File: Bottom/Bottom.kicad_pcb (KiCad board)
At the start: 2 copper layers, 40 x 40 mm, 32 parts, among them M1 Motor, M2 Motor, U1 GP2S60, U2 GP2S60, U7 DRV8833PWP

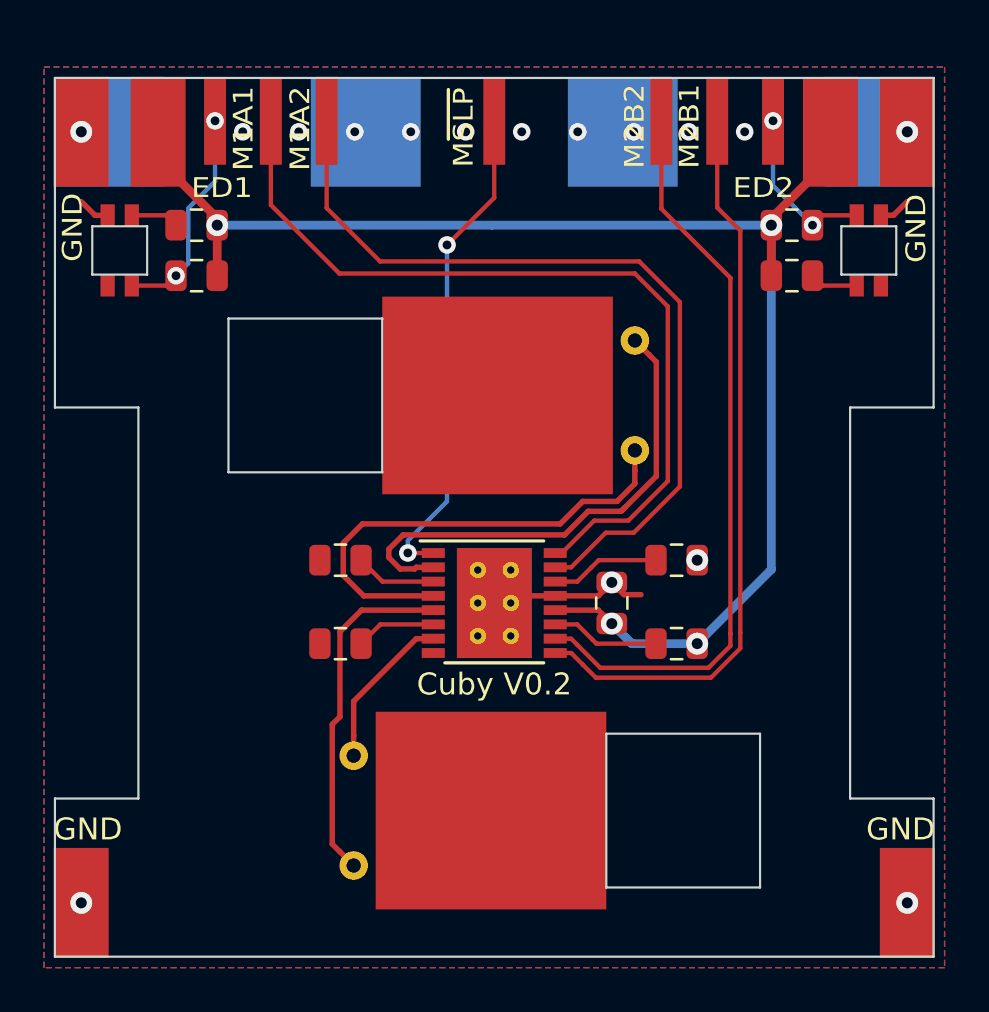
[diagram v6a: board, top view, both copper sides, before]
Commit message: removed extra pins in front, respaced pins in bottom and front
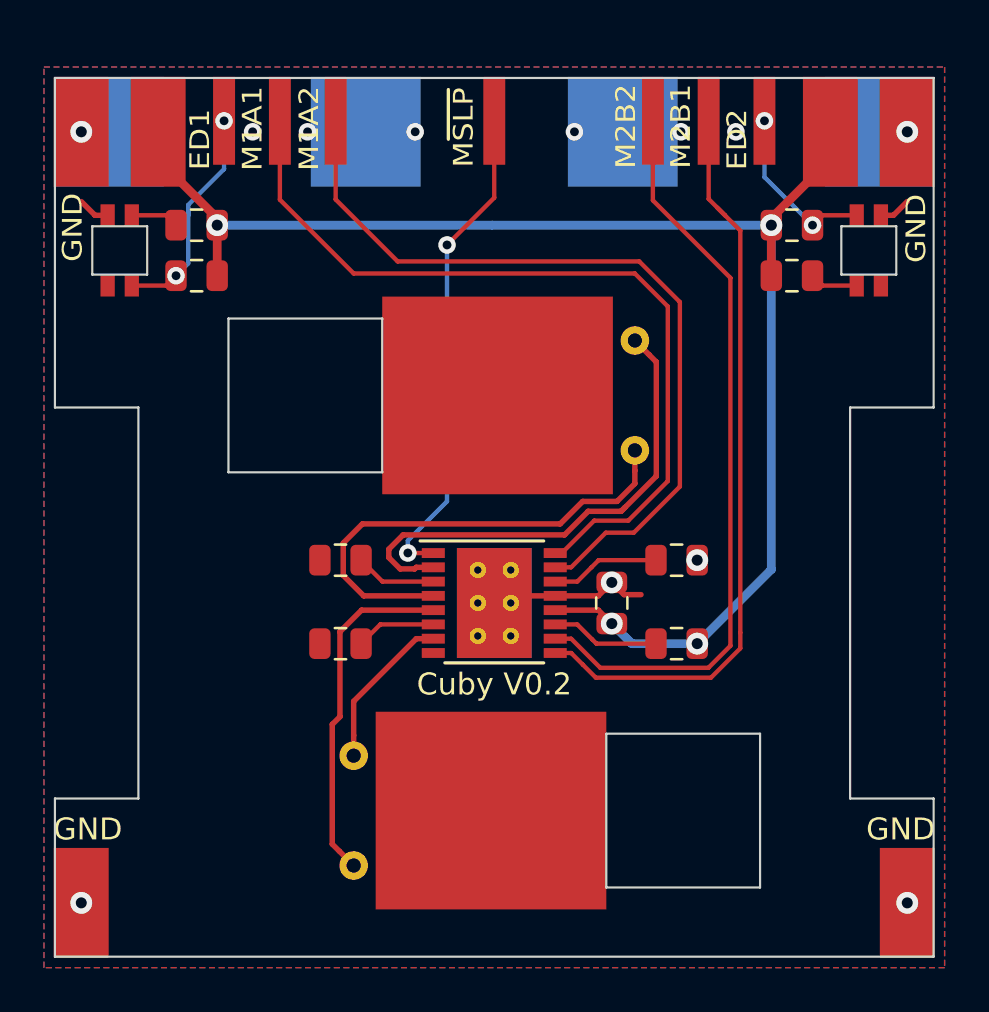
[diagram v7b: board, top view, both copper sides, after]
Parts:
- moved H1 0.41 mm to (163.2, 80.0)
- moved H2 0.41 mm to (165.8, 80.0)
- moved H5 0.41 mm to (160.7, 80.0)
- moved H3 0.39 mm to (182.8, 80.0)
- moved H4 0.39 mm to (180.2, 80.0)
- moved H6 0.39 mm to (185.3, 80.0)
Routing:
- net /M1_AIN2: track 38.9 -> 36.8 mm
- net /M2_BIN1: track 33.9 -> 34.5 mm
- net /M1_AIN1: track 38.2 -> 37.7 mm
- net Net-(H5-Pad1): track 9.99 -> 10.5 mm
- net GND: vias 16 -> 12
